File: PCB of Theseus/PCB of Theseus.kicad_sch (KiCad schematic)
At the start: 43 parts, among them J1 Screw_Terminal_01x04, J2 Screw_Terminal_01x04, J4 Screw_Terminal_01x06, J7 Screw_Terminal_01x02, J8 Screw_Terminal_01x06, Q1 NMOS, Q2 NMOS, U1 TPS564257DRL, U2 MCP2562

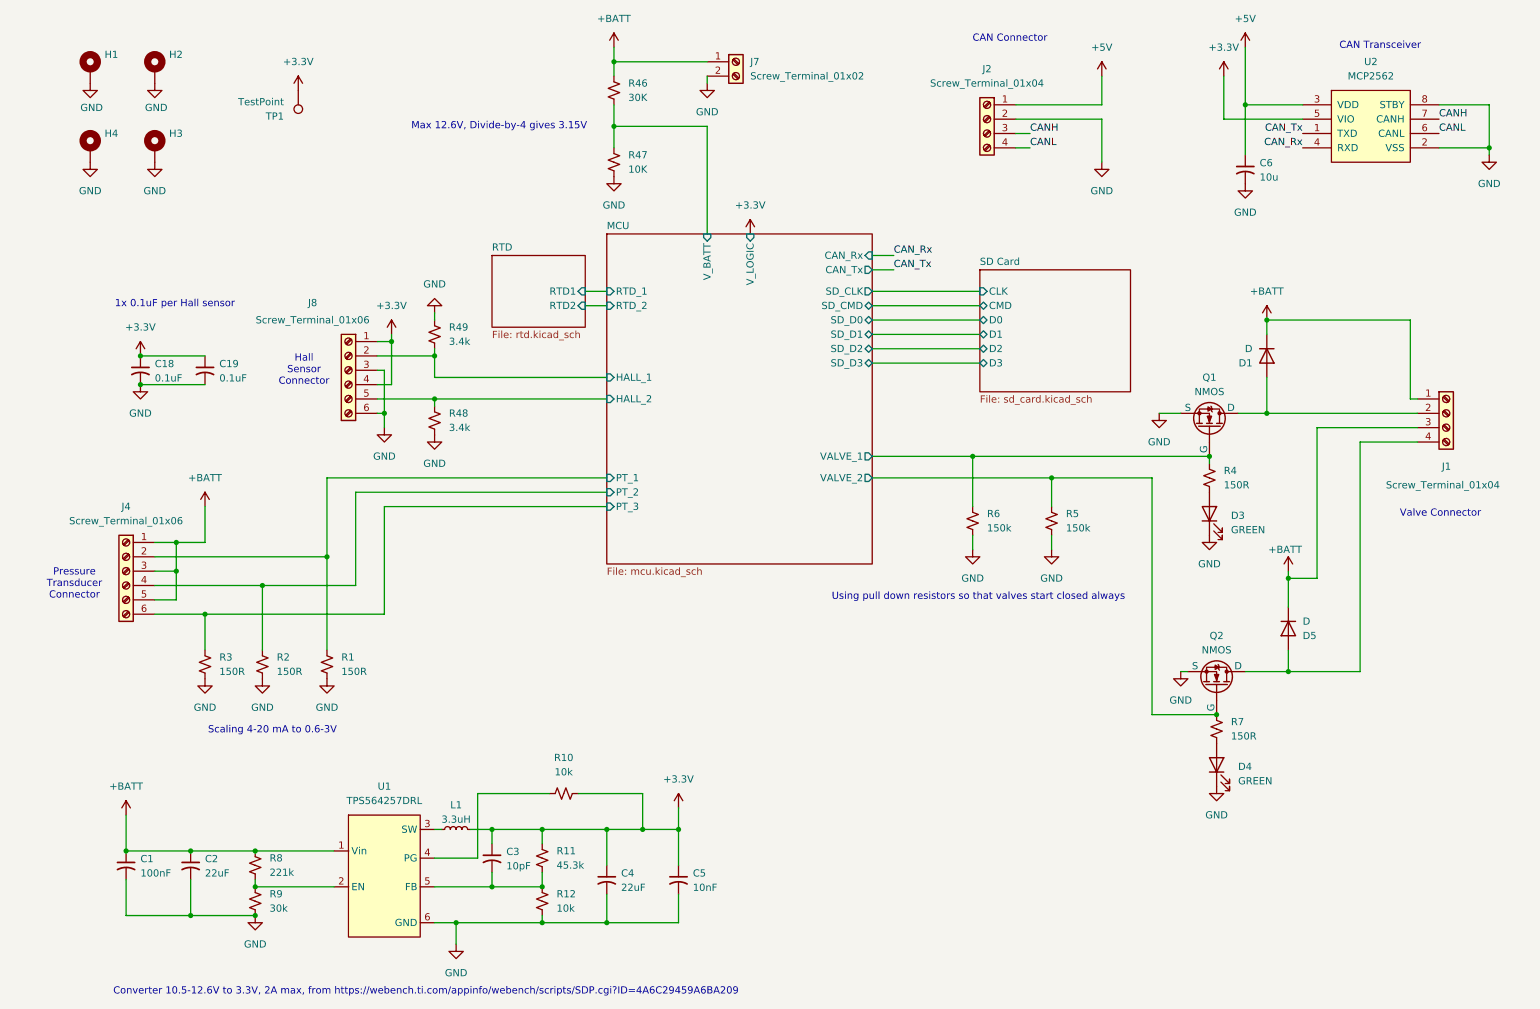
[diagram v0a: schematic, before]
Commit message: Updates to schematic, added 3rd RTD, initial PCB layout completed.
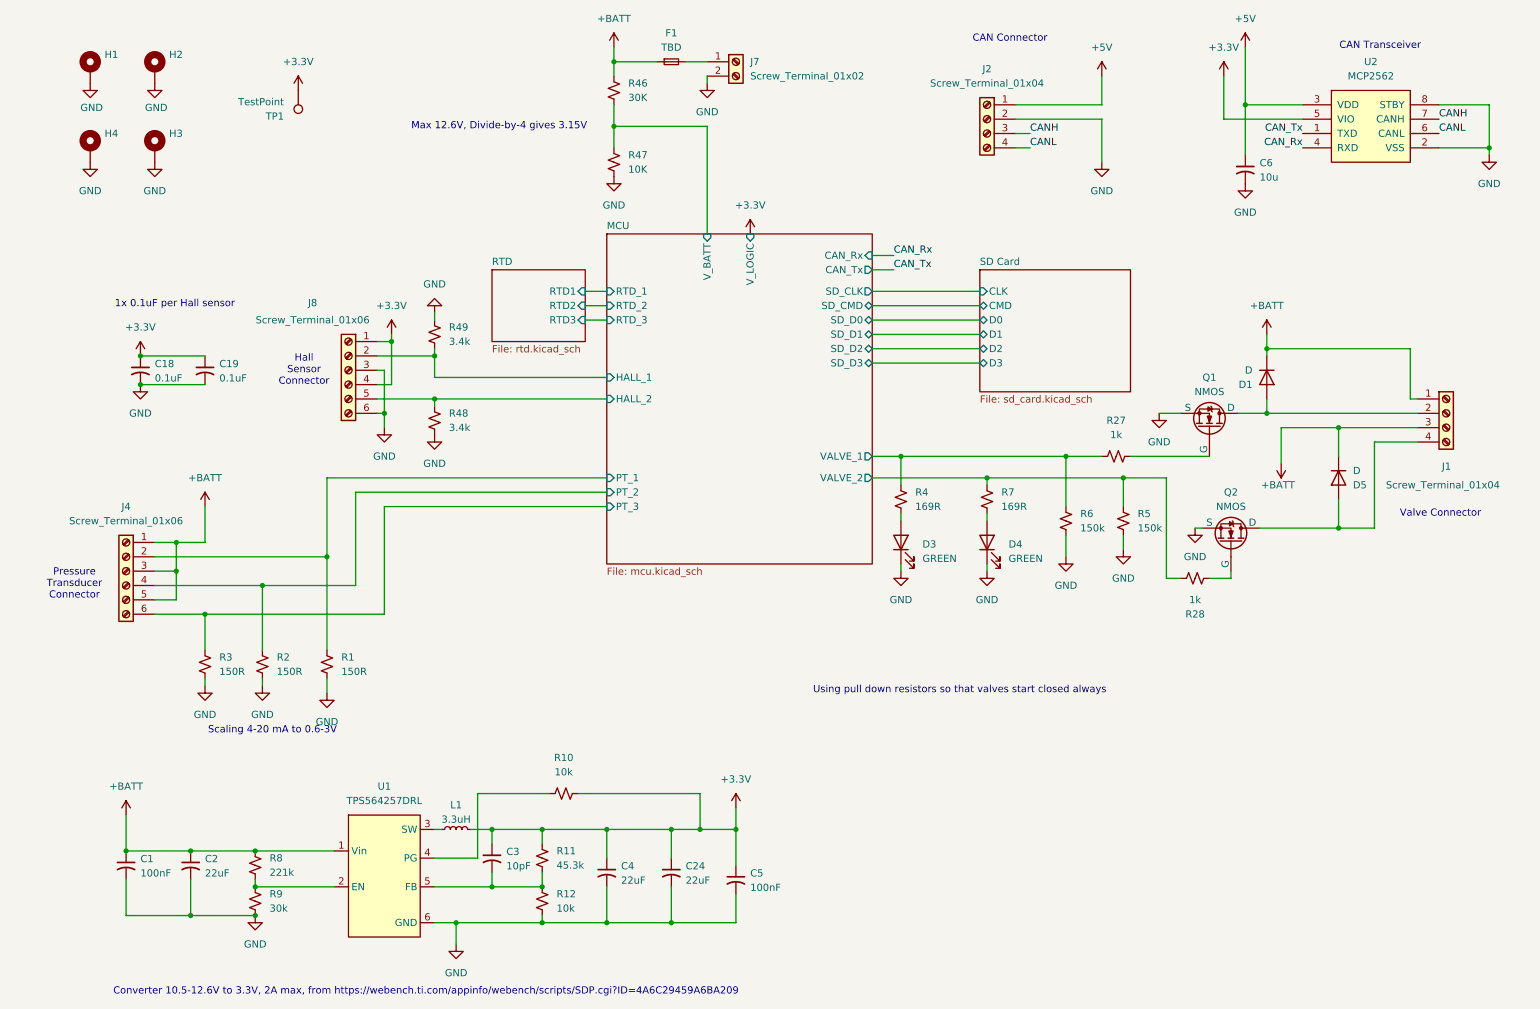
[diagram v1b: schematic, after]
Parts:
- added C24: 22uF, Capacitor_SMD:C_0805_2012Metric_Pad1.18x1.45mm_HandSolder, symbol Device:C_Small_US
- added F1: TBD, Fuse:Fuse_1206_3216Metric_Pad1.42x1.75mm_HandSolder, symbol Device:Fuse_Small
- added R27, R28: 1k, Resistor_SMD:R_0402_1005Metric_Pad0.72x0.64mm_HandSolder, symbol Device:R_Small_US
- C1, C6: footprint (none) -> Capacitor_SMD:C_0603_1608Metric_Pad1.08x0.95mm_HandSolder
- C18, C19: footprint (none) -> Capacitor_SMD:C_0201_0603Metric_Pad0.64x0.40mm_HandSolder
- C2, C4: footprint (none) -> Capacitor_SMD:C_0805_2012Metric_Pad1.18x1.45mm_HandSolder
- C3: footprint (none) -> Capacitor_SMD:C_0402_1005Metric_Pad0.74x0.62mm_HandSolder
- C5: value 10nF -> 100nF; footprint (none) -> Capacitor_SMD:C_0603_1608Metric_Pad1.08x0.95mm_HandSolder
- D1, D5: footprint (none) -> Diode_SMD:D_SMB-SMC_Universal_Handsoldering
- D3, D4: footprint (none) -> Diode_SMD:D_0603_1608Metric_Pad1.05x0.95mm_HandSolder
- H1, H2, H3, H4: footprint (none) -> MountingHole:MountingHole_3.2mm_M3_Pad_Via
- J1, J2: footprint (none) -> TerminalBlock_CUI:TerminalBlock_CUI_TB007-508-04_1x04_P5.08mm_Horizontal
- J4, J8: footprint (none) -> TerminalBlock_CUI:TerminalBlock_CUI_TB007-508-06_1x06_P5.08mm_Horizontal
- J7: footprint (none) -> TerminalBlock_CUI:TerminalBlock_CUI_TB007-508-02_1x02_P5.08mm_Horizontal
- L1: footprint (none) -> Fydp_footprints:VLS6045EX-3R3N
- Q1, Q2: footprint (none) -> Package_TO_SOT_SMD:SOT-23-3
- R1, R11, R2, R3, R46, R5, R6, R8, R9: footprint (none) -> Resistor_SMD:R_0603_1608Metric_Pad0.98x0.95mm_HandSolder
- R10, R12, R47, R48, R49: footprint (none) -> Resistor_SMD:R_0402_1005Metric_Pad0.72x0.64mm_HandSolder
- R4, R7: value 150R -> 169R; footprint (none) -> Resistor_SMD:R_0603_1608Metric_Pad0.98x0.95mm_HandSolder
- TP1: footprint (none) -> TestPoint:TestPoint_Pad_D2.0mm
- U1: footprint (none) -> Package_TO_SOT_SMD:SOT-563
- U2: footprint (none) -> Package_SO:SOIC-8_3.9x4.9mm_P1.27mm
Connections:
- net +3.3V: now also C24.1
- net +BATT: now also F1.1; no longer J7.1 (Pin_1)
- net GND: now also C24.2
- net MCU/VALVE_1: now also R27.2; no longer Q1.2 (G)
- net MCU/VALVE_2: now also R28.2; no longer Q2.2 (G)
- new net: Q1.2 (G), R27.1
- new net: F1.2, J7.1 (Pin_1)
- new net: Q2.2 (G), R28.1
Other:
- sheet MCU ports: added RTD_3; removed none
- sheet RTD ports: added RTD3; removed none
- moved on the sheet: C4, C5, D1, D3, D4, D5, Q2, R4, R5, R6, R7
